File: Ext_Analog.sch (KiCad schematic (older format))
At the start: 27 parts

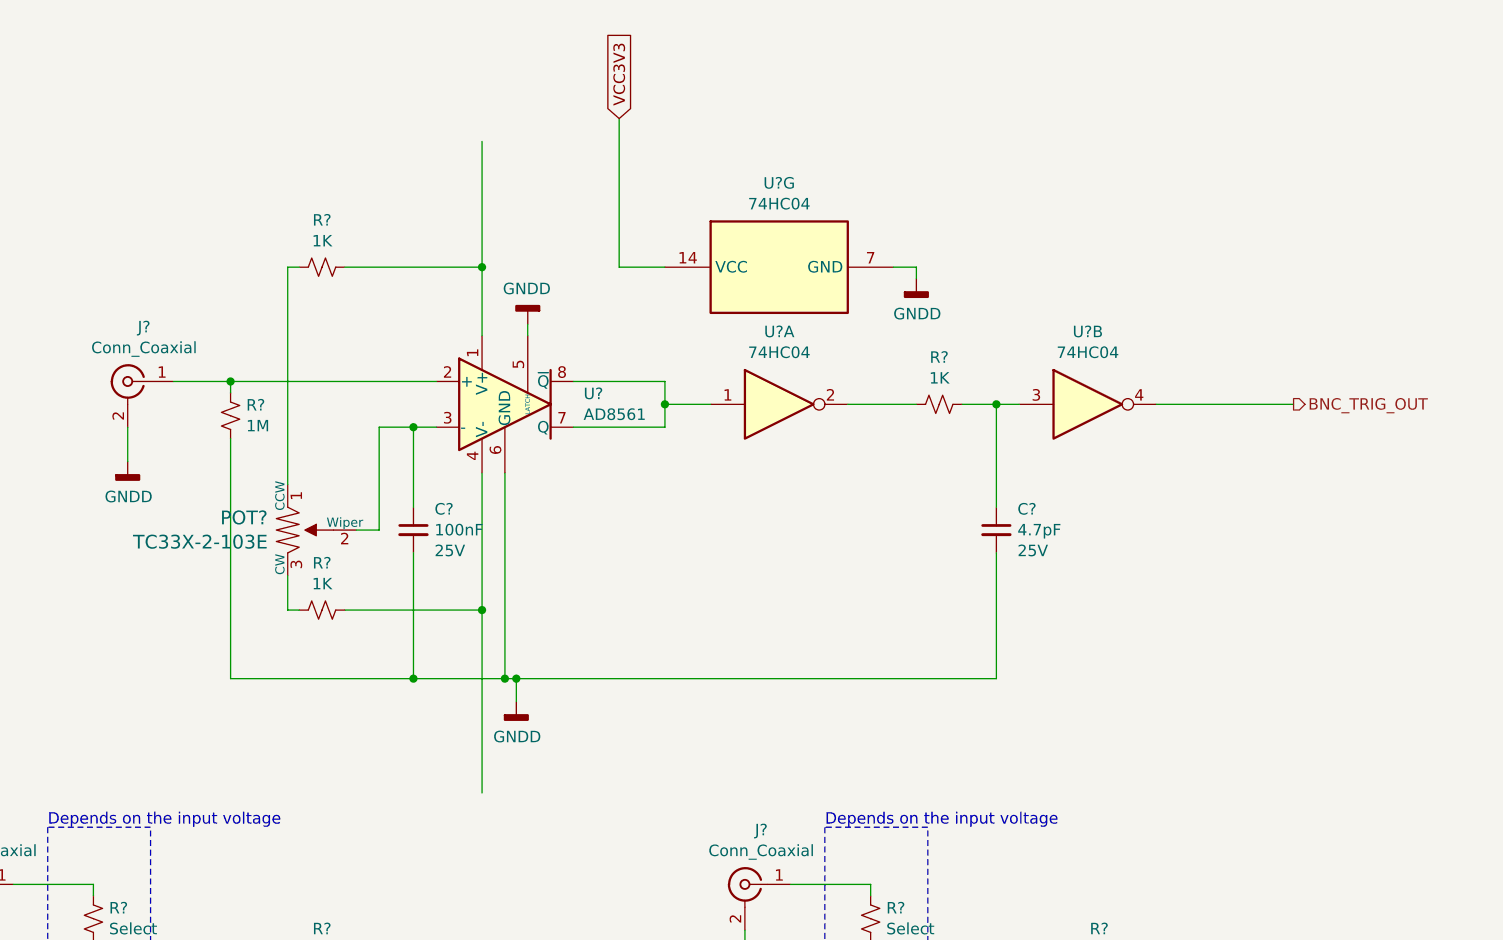
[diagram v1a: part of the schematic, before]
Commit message: Added nets for fx3 usb3 cct from fpga
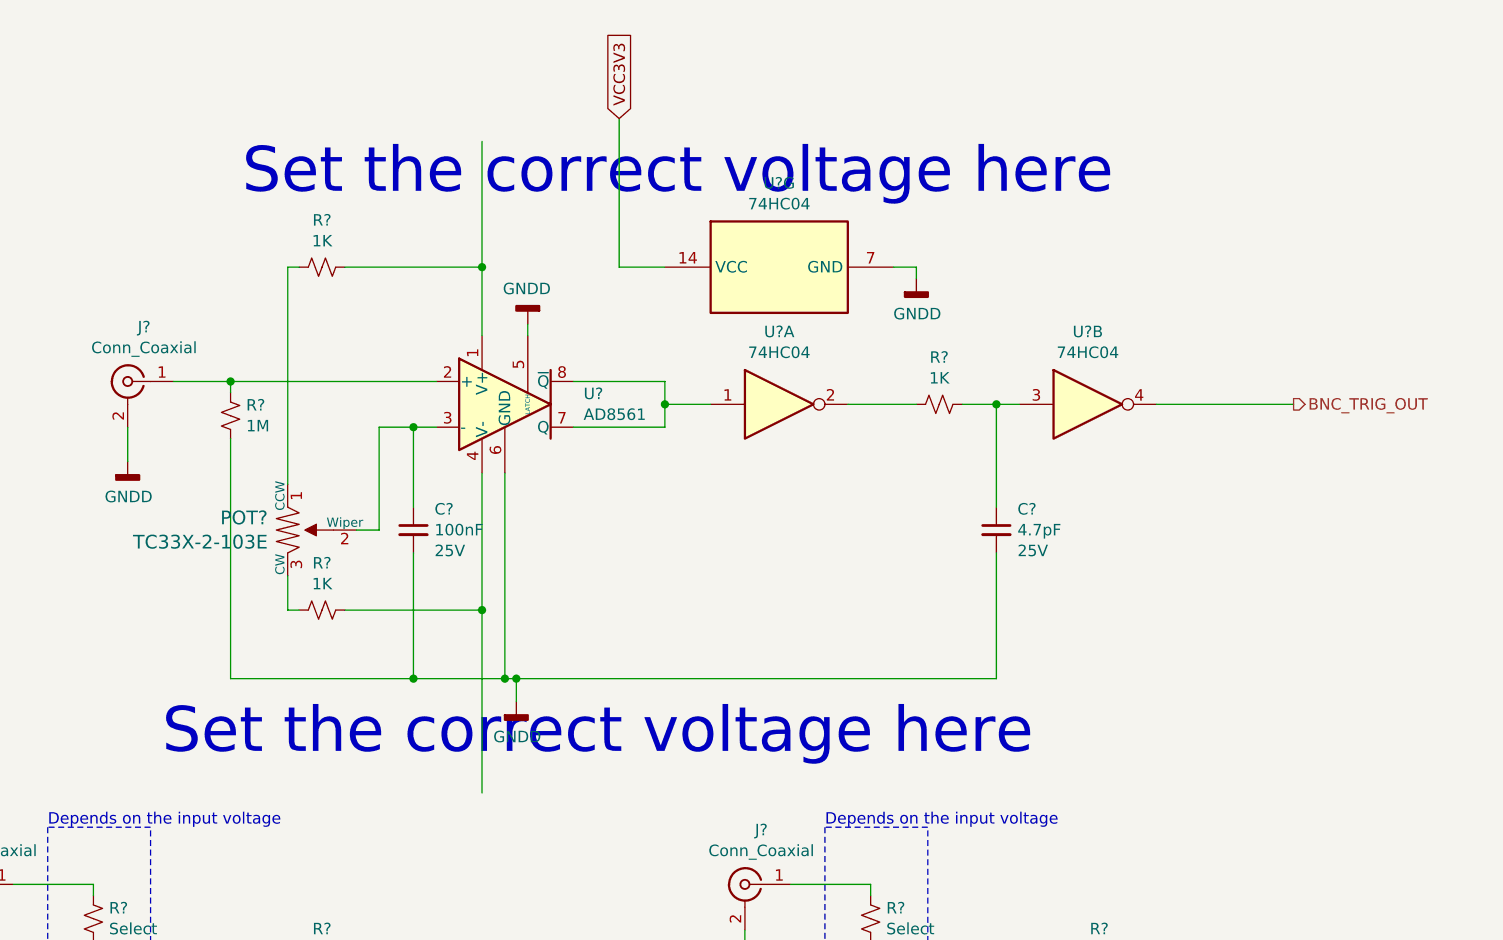
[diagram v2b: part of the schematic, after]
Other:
- note added: "Set the correct voltage here"
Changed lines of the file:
@@
 $Descr A4 11693 8268
 encoding utf-8
-Sheet 17 22
+Sheet 16 22
 Title ""
 Date ""
@@
 Text HLabel 9250 5150 2    50   Output ~ 0
 AN1_N
+Text Notes 4150 1350 0    197  ~ 0
+Set the correct voltage here
+Text Notes 3800 3800 0    197  ~ 0
+Set the correct voltage here
 $EndSCHEMATC

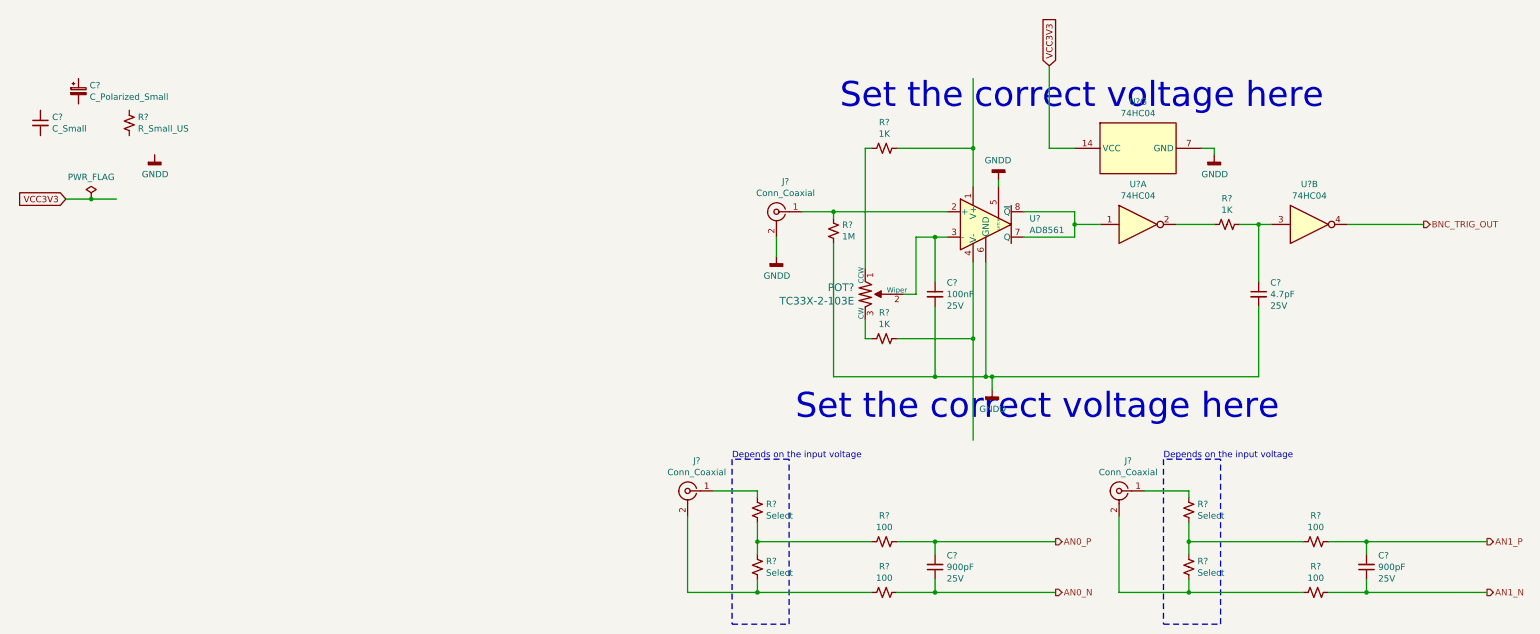
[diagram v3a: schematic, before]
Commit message: PCB created and schematics annotated High speed connections added to the BTB
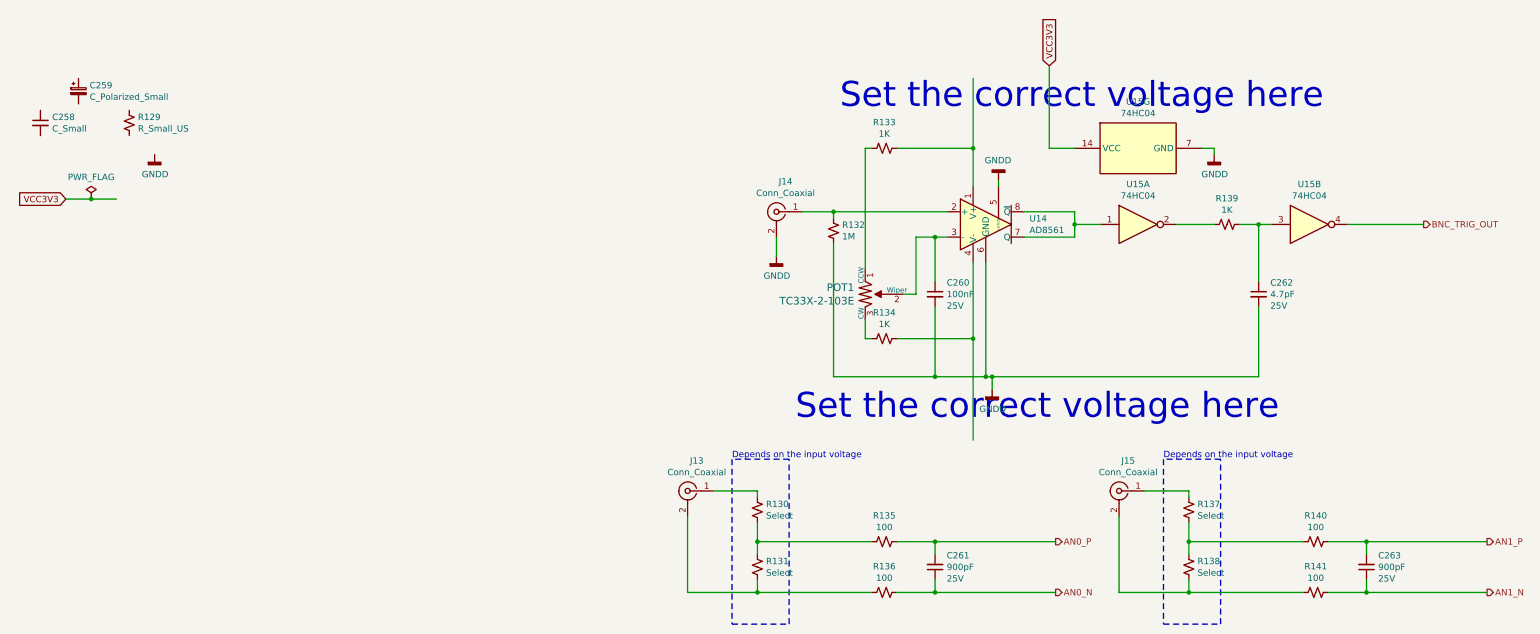
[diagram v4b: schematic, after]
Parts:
- gave numbers to parts that had none: 25

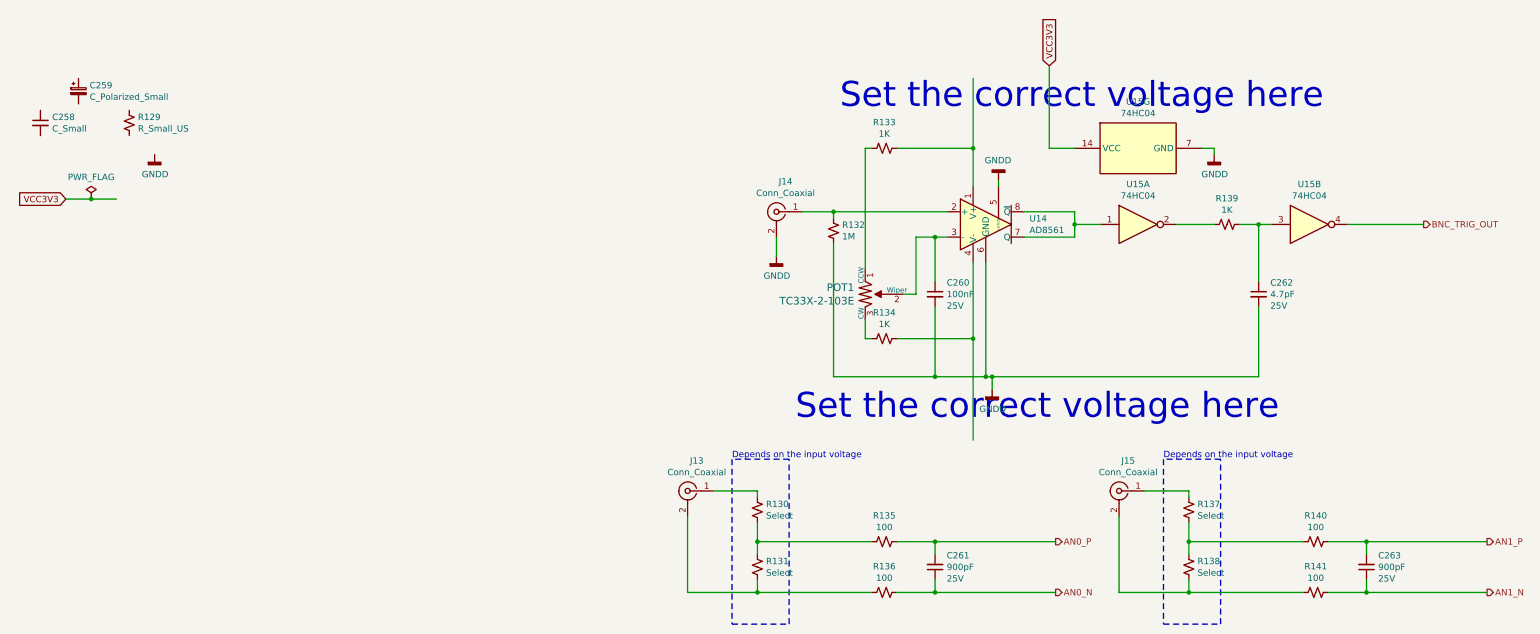
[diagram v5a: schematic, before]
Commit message: Corrected PCB import errors
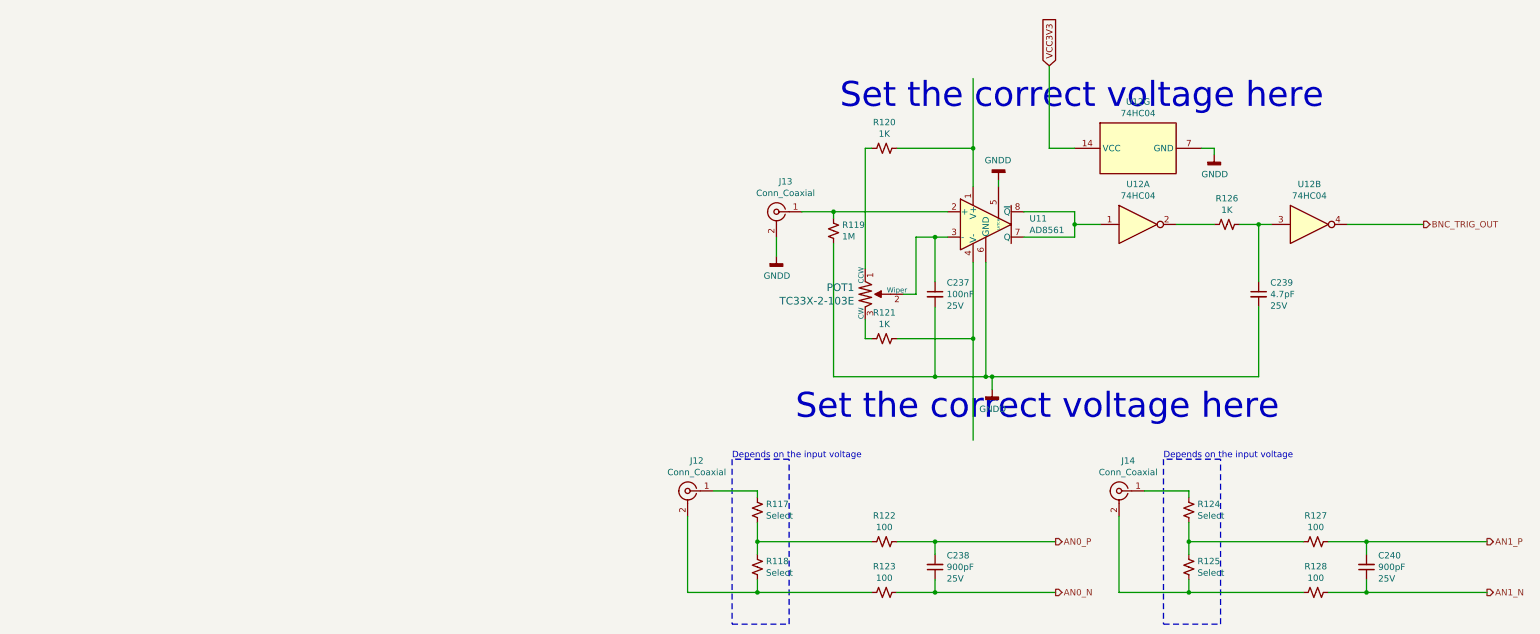
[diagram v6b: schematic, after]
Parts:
- removed C258: C_Small, Capacitor_SMD:C_0603_1608Metric_Pad1.08x0.95mm_HandSolder, symbol Device:C_Small
- removed C259: C_Polarized_Small, Capacitor_Tantalum_SMD:CP_EIA-1608-10_AVX-L_Pad1.25x1.05mm_HandSolder, symbol Device:C_Polarized_Small
- removed R129: R_Small_US, Resistor_SMD:R_0603_1608Metric_Pad0.98x0.95mm_HandSolder, symbol Device:R_Small_US
- renumbered C260 to C237, C261 to C238, C262 to C239, C263 to C240, J13 to J12, J14 to J13, J15 to J14, R130 to R117, R131 to R118, R132 to R119, R133 to R120, R134 to R121, R135 to R122, R136 to R123, R137 to R124, R138 to R125, R139 to R126, R140 to R127, R141 to R128, U14 to U11, U15 to U12
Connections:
- wire segments 75 -> 73
